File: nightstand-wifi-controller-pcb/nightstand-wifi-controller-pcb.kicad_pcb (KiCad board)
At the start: 2 copper layers, 67.4 x 57.2 mm, 8 parts, among them J2 Conn_01x06_Socket, J4 Screw_Terminal_01x02, J5 Screw_Terminal_01x02, K2 FINDER-36.11, Q2 PN2222A

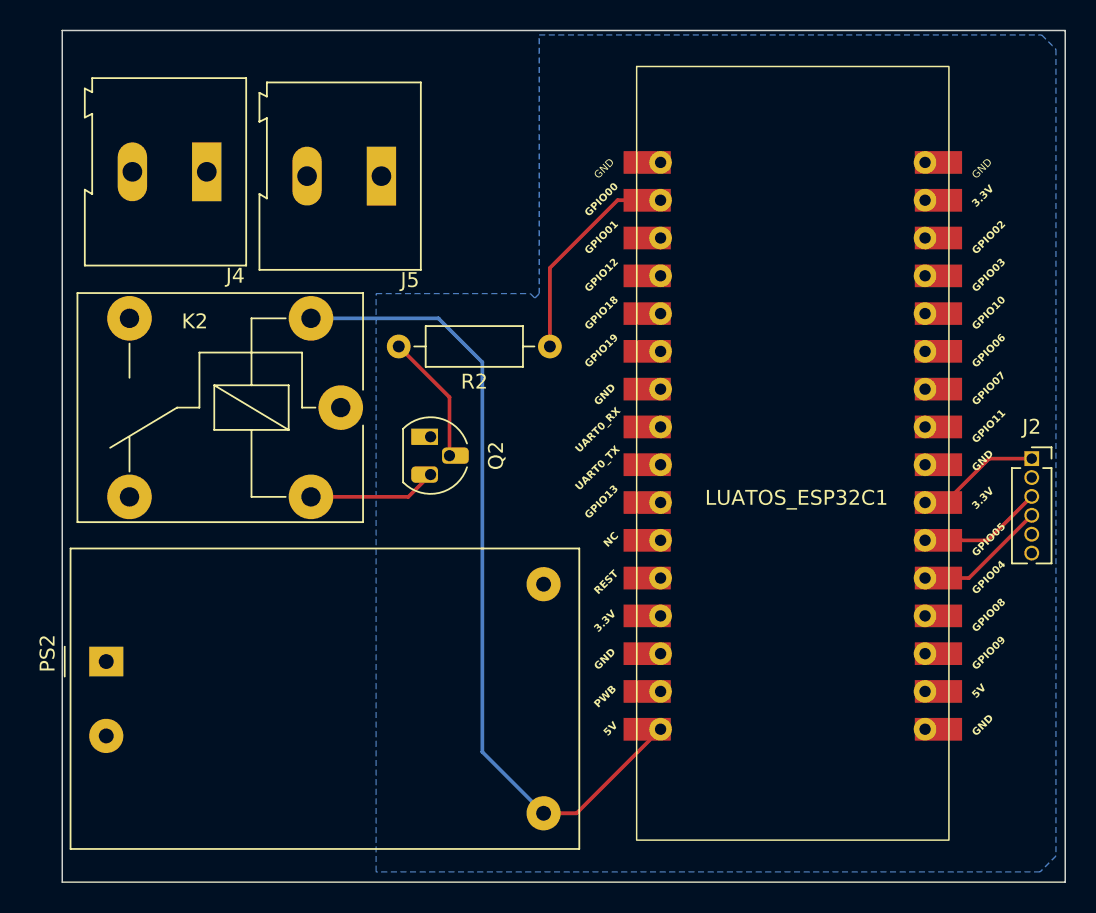
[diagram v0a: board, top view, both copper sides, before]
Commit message: PCB design completeed and JLCPCB Design rules set up
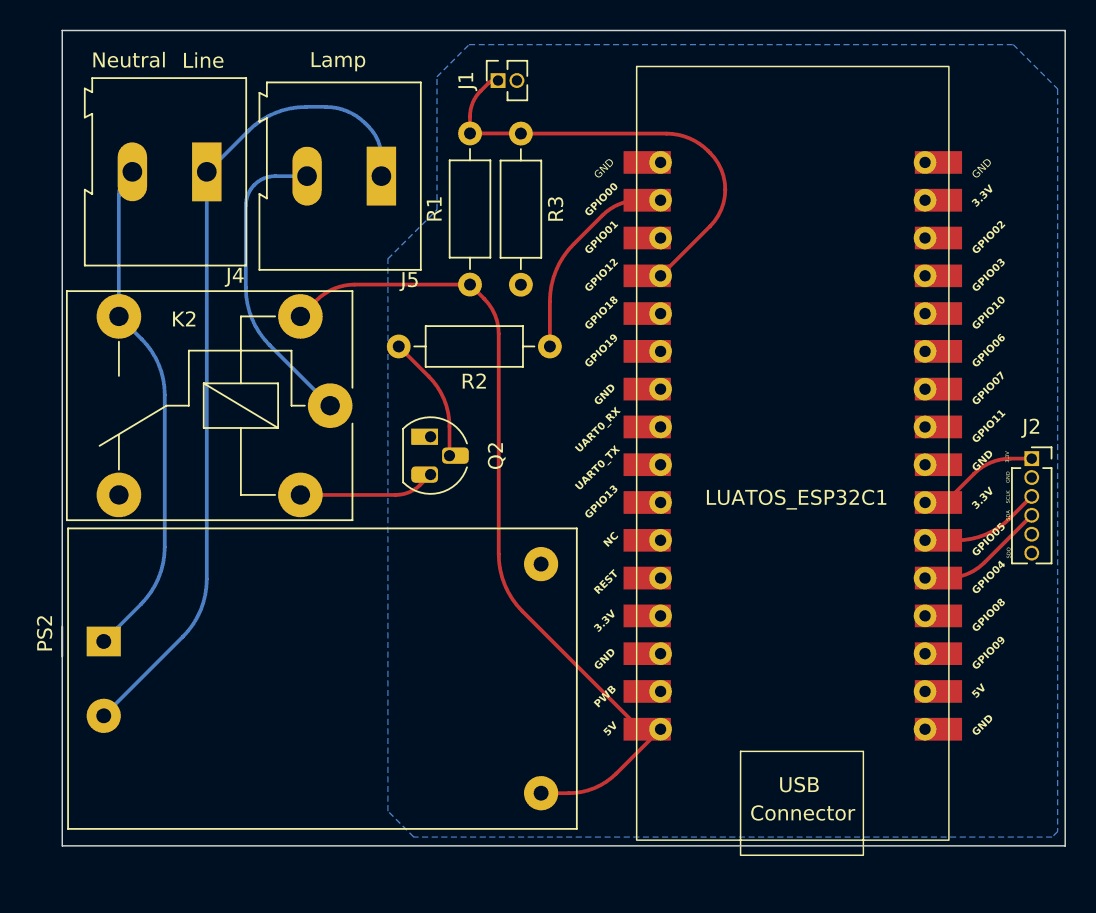
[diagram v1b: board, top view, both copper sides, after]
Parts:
- added J1: Conn_01x02_Socket, Connector_PinSocket_1.27mm:PinSocket_1x02_P1.27mm_Vertical, F.Cu at (110.8, 62.7)
- added R1: 10M Omh, Resistor_THT:R_Axial_DIN0207_L6.3mm_D2.5mm_P10.16mm_Horizontal, F.Cu at (108.9, 76.4)
- added R3: 15M Omh, Resistor_THT:R_Axial_DIN0207_L6.3mm_D2.5mm_P10.16mm_Horizontal, F.Cu at (112.3, 66.2)
- moved PS2 1.36 mm to (84.3, 100.4)
- moved K2 0.72 mm to (99.5, 84.5)
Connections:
- J2 pad 2: Net-(J2-Pin_2) -> GND
- J2 pad 6: Net-(J2-Pin_2) -> GND
- LUATOS_ESP32C1 pad 25: Net-(J2-Pin_2) -> GND
- LUATOS_ESP32C1 pad 32: GND -> unconnected-(LUATOS_ESP32C1-GND-Pad32)
- LUATOS_ESP32C1 pad 4: unconnected-(LUATOS_ESP32C1-GPIO12-Pad4) -> Net-(J1-Pin_1)
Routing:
- net Net-(J4-Pin_1): track 0.00 -> 55.5 mm
- net Net-(J4-Pin_2): track 0.00 -> 34.3 mm
- net Net-(J1-Pin_1): track 0.00 -> 31.1 mm
- net Net-(J5-Pin_2): track 0.00 -> 20.8 mm
- net Net-(PS2-+Vout): track 55.0 -> 57.2 mm
- net Net-(Q2-C): track 8.66 -> 9.21 mm
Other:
- board size 67.4 x 57.2 mm -> 67.4 x 54.8 mm
- board text added: "3.3V"
- board text added: "GND"
- board text added: "Lamp"
- board text added: "Line"
- board text added: "Neutral"
- board text added: "SCLK"
- board text added: "SDA"
- board text added: "SDO"

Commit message: Header pin sizes fixed from 1.27mm to 2.54mm
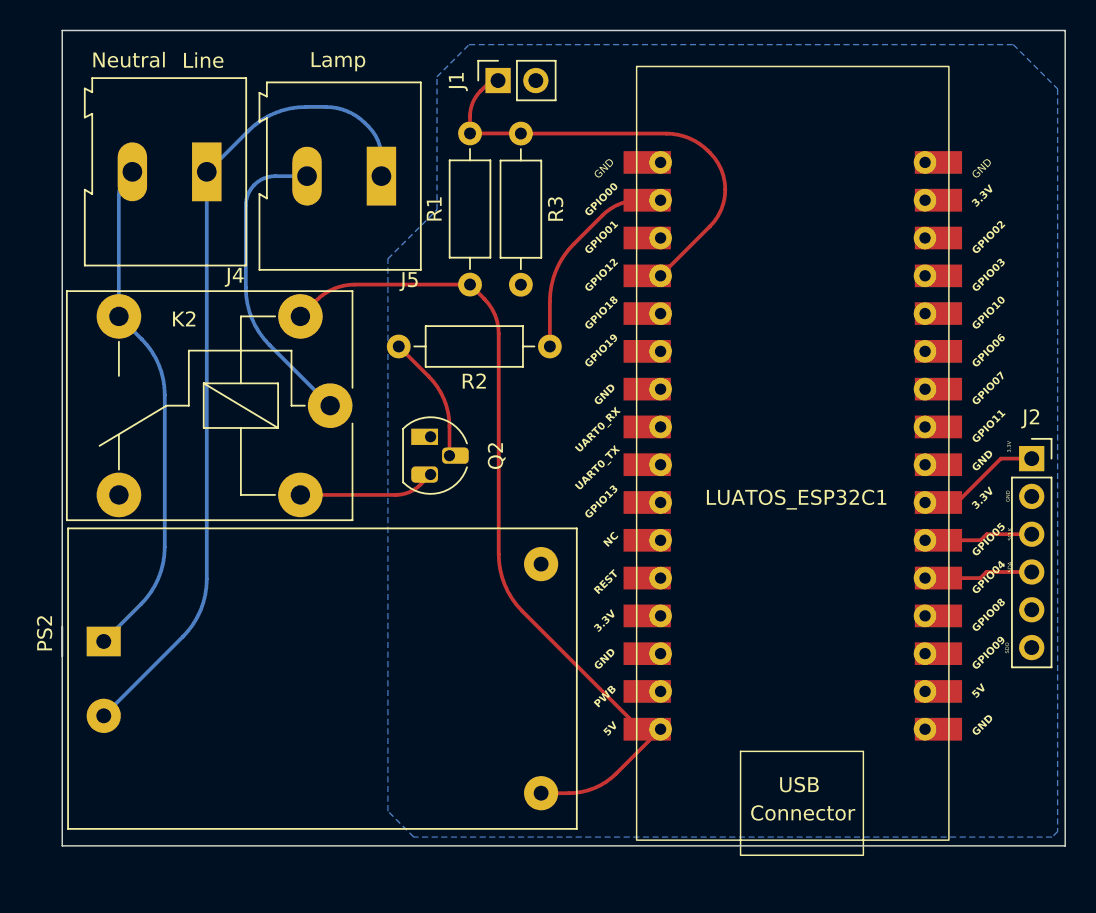
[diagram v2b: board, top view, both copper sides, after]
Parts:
- J1: footprint Connector_PinSocket_1.27mm:PinSocket_1x02_P1.27mm_Vertical -> Connector_PinSocket_2.54mm:PinSocket_1x02_P2.54mm_Vertical
- J2: footprint Connector_PinSocket_1.27mm:PinSocket_1x06_P1.27mm_Vertical -> Connector_PinSocket_2.54mm:PinSocket_1x06_P2.54mm_Vertical
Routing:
- net Net-(J2-Pin_4): track 8.75 -> 7.34 mm
- net Net-(J2-Pin_3): track 8.15 -> 7.34 mm
